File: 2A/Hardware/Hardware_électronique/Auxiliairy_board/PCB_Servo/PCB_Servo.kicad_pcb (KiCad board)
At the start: 2 copper layers, 38.8 x 40.2 mm, 35 parts, among them J10 Conn_ST_STDC14, J9 UART_IN, U1 STM32G071CBUx, U2 AZ1117-3.3

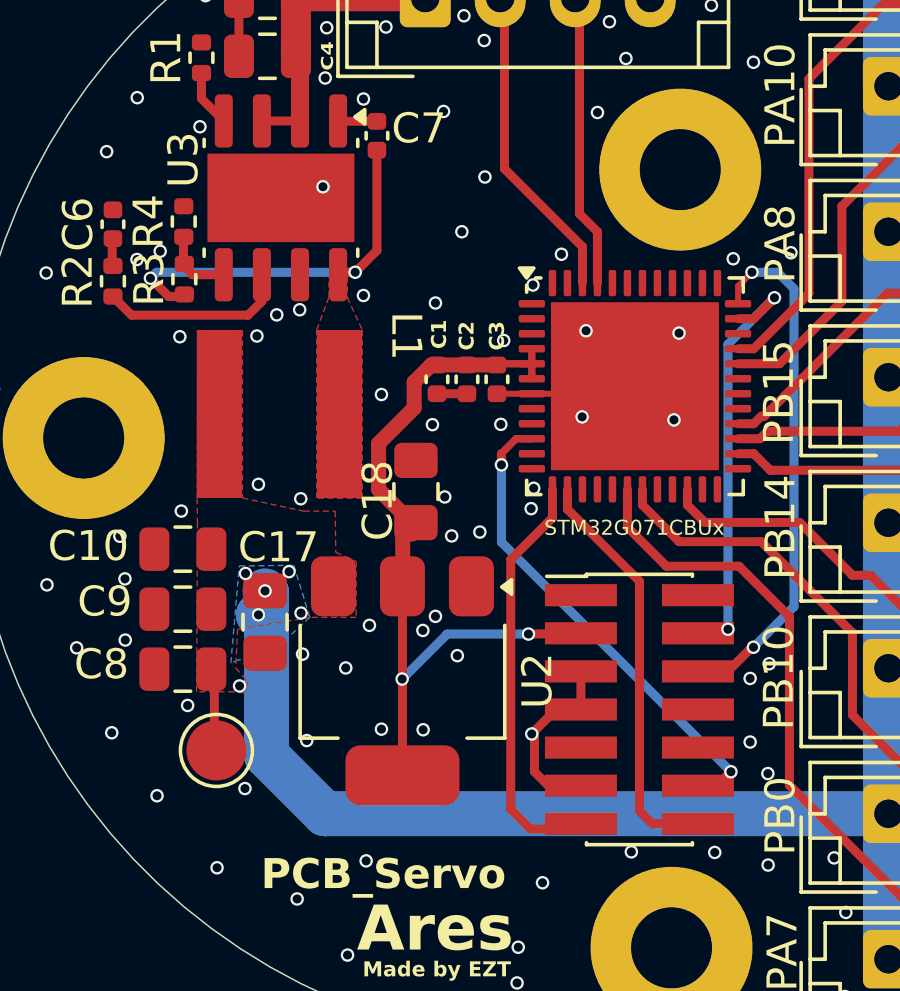
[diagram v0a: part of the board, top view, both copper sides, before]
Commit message: Correction PCB Servo LF
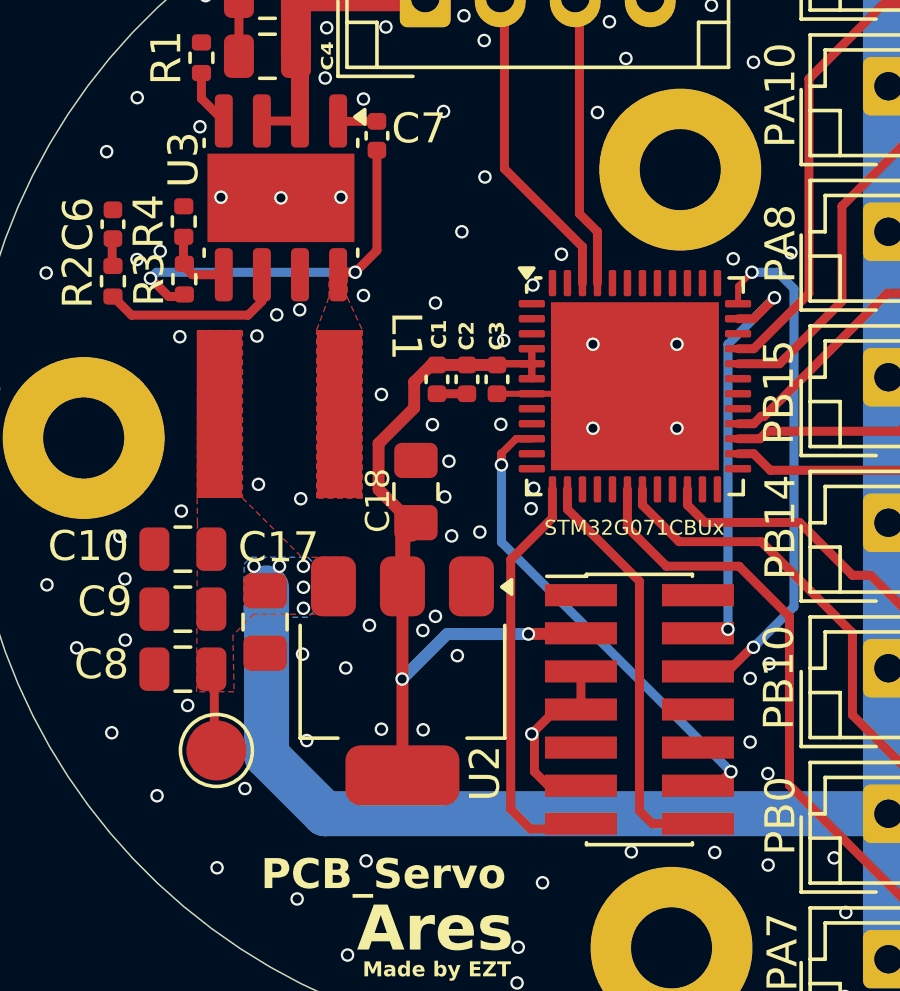
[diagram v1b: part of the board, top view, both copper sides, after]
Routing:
- net +7.5V: track 64.8 -> 64.7 mm, vias 6 -> 5
- net GND: vias 174 -> 177
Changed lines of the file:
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@@
 			(effects
 				(font
-					(size 1 1)
-					(thickness 0.15)
+					(size 0.8 0.8)
+					(thickness 0.13)
 				)
 			)
@@
 		(tags "CMS SOT")
 		(property "Reference" "U2"
-			(at 0 -4.5 90)
+			(at 3.08 -2.75 90)
 			(layer "F.SilkS")
 			(effects
@@
 	)
 	(via
+		(at 137.4 66.8)
+		(size 0.45)
+		(drill 0.3)
+		(layers "F.Cu" "B.Cu")
+		(free yes)
+		(net 1)
+	)
+	(via
 		(at 136.875 62.825)
 		(size 0.45)
@@
 	)
 	(via
-		(at 148.67 71.33)
+		(at 148.6 71.7)
 		(size 0.45)
 		(drill 0.3)
@@
 	)
 	(via
+		(at 133.4 66.8)
+		(size 0.45)
+		(drill 0.3)
+		(layers "F.Cu" "B.Cu")
+		(free yes)
+		(net 1)
+	)
+	(via
 		(at 129.59 65.28)
 		(size 0.45)
@@
 	)
 	(via
+		(at 141 75.6)
+		(size 0.45)
+		(drill 0.3)
+		(layers "F.Cu" "B.Cu")
+		(free yes)
+		(net 1)
+	)
+	(via
 		(at 144.95 58.7)
 		(size 0.45)
@@
 	)
 	(via
-		(at 148.5 74.22)
+		(at 148.6 74.5)
 		(size 0.45)
 		(drill 0.3)
@@
 	)
 	(via
-		(at 136.8 66.45)
+		(at 135.4 66.82)
 		(size 0.45)
 		(drill 0.3)
@@
 	)
 	(via
-		(at 145.44 74.12)
+		(at 145.8 74.5)
 		(size 0.45)
 		(drill 0.3)
@@
 	)
 	(via
-		(at 145.57 71.25)
+		(at 145.8 71.7)
 		(size 0.45)
 		(drill 0.3)
@@
 		(start 145.4 81.335)
 		(end 143.65 81.36)
-		(width 0.3)
+		(width 0.4)
 		(layer "F.Cu")
 		(net 2)
@@
 		(start 138.655 75.008122)
 		(end 138.655 76.5425)
-		(width 0.5)
+		(width 0.4)
 		(layer "F.Cu")
 		(net 2)
@@
 		(start 139.45 82.87)
 		(end 139.44 82.86)
-		(width 0.3)
+		(width 0.4)
 		(layer "F.Cu")
 		(net 2)
@@
 		(start 139.45 82.85)
 		(end 139.45 79.77)
-		(width 0.3)
+		(width 0.4)
 		(layer "F.Cu")
 		(net 2)
@@
 		(start 139.84 72.961734)
 		(end 139.84 73.823122)
-		(width 0.5)
+		(width 0.4)
 		(layer "F.Cu")
 		(net 2)
@@
 		(start 143.645 81.335)
 		(end 143.64 81.33)
-		(width 0.3)
+		(width 0.4)
 		(layer "F.Cu")
 		(net 2)
@@
 		(start 140.411734 72.39)
 		(end 139.84 72.961734)
-		(width 0.5)
+		(width 0.4)
 		(layer "F.Cu")
 		(net 2)
@@
 		(start 138.655 76.5425)
 		(end 139.83 77.7175)
-		(width 0.5)
+		(width 0.4)
 		(layer "F.Cu")
 		(net 2)
@@
 		(start 139.44 82.86)
 		(end 139.45 82.85)
-		(width 0.3)
+		(width 0.4)
 		(layer "F.Cu")
 		(net 2)
@@
 		(start 139.84 73.823122)
 		(end 138.655 75.008122)
-		(width 0.5)
+		(width 0.4)
 		(layer "F.Cu")
 		(net 2)
@@
 		(start 143.65 81.36)
 		(end 143.645 81.335)
-		(width 0.3)
+		(width 0.4)
 		(layer "F.Cu")
 		(net 2)
@@
 		(start 139.45 86.07)
 		(end 139.45 82.87)
-		(width 0.3)
+		(width 0.4)
 		(layer "F.Cu")
 		(net 2)
@@
 		(start 140.6 72.39)
 		(end 142.6 72.39)
-		(width 0.5)
+		(width 0.4)
 		(layer "F.Cu")
 		(net 2)
@@
 		(start 140.6 72.39)
 		(end 140.411734 72.39)
-		(width 0.5)
+		(width 0.4)
 		(layer "F.Cu")
 		(net 2)
@@
 		(start 143.65 81.36)
 		(end 140.94 81.36)
-		(width 0.3)
+		(width 0.4)
 		(layer "B.Cu")
 		(net 2)
@@
 		(start 140.94 81.36)
 		(end 139.44 82.86)
-		(width 0.3)
+		(width 0.4)
 		(layer "B.Cu")
 		(net 2)
@@
 	)
 	(via
-		(at 134.02 83.09)
-		(size 0.45)
-		(drill 0.3)
-		(layers "F.Cu" "B.Cu")
-		(free yes)
-		(net 59)
-	)
-	(via
-		(at 134.22 79.34)
+		(at 134.5 79.1)
 		(size 0.45)
 		(drill 0.3)
@@
 	)
 	(via
-		(at 134.87 79.9225)
+		(at 136.15 79.8)
 		(size 0.45)
 		(drill 0.3)
@@
 	)
 	(via
-		(at 135.67 79.28)
+		(at 136.15 79.1)
 		(size 0.45)
 		(drill 0.3)
@@
 	)
 	(via
-		(at 134.65 80.72)
+		(at 135.35 79.1)
 		(size 0.45)
 		(drill 0.3)
@@
 	)
 	(via
-		(at 136.07 80.66)
+		(at 136.15 80.5)
 		(size 0.45)
 		(drill 0.3)
@@
 	)
 	(segment
-		(start 134.92 80.45)
-		(end 134.65 80.72)
-		(width 1.5)
-		(layer "B.Cu")
-		(net 59)
-	)
-	(segment
 		(start 155.65 82.5)
 		(end 155.65 92.2)
@@
 	)
 	(segment
-		(start 134.87 79.9225)
-		(end 134.92 79.9725)
-		(width 1.5)
-		(layer "B.Cu")
-		(net 59)
-	)
-	(segment
 		(start 155.65 70.95)
 		(end 155.65 74.6)
@@
 	)
 	(segment
-		(start 134.92 80.99)
-		(end 134.92 85.406701)
-		(width 1.5)
-		(layer "B.Cu")
-		(net 59)
-	)
-	(segment
 		(start 134.92 85.406701)
 		(end 136.863299 87.35)
@@
 	)
 	(segment
-		(start 134.92 79.9725)
-		(end 134.92 80.45)
+		(start 134.92 85.406701)
+		(end 134.92 79.82)
 		(width 1.5)
 		(layer "B.Cu")
@@
 		(net 59)
 	)
-	(segment
-		(start 134.65 80.72)
-		(end 134.92 80.99)
-		(width 1.5)
-		(layer "B.Cu")
-		(net 59)
-	)
 	(zone
 		(net 54)
@@
 		(polygon
 			(pts
-				(xy 134.11729 71.243864) (xy 134.11729 76.823864) (xy 136.15729 77.263864) (xy 137.20729 77.263864)
-				(xy 137.22729 78.633864) (xy 137.90729 78.943864) (xy 137.90729 80.803864) (xy 136.38729 80.803864)
-				(xy 133.95729 81.193864) (xy 133.89 82.49) (xy 134.29 82.94) (xy 134.18 83.32) (xy 133.83729 83.283864)
-				(xy 132.58729 83.283864) (xy 132.61729 77.673864) (xy 132.60729 76.813864) (xy 132.62729 71.243864)
+				(xy 134.11729 71.243864) (xy 134.11729 76.823864) (xy 136.1 78.8) (xy 137.5 78.8) (xy 137.5 80.7)
+				(xy 134.5 80.7) (xy 133.8 81.4) (xy 133.83729 83.283864) (xy 132.58729 83.283864) (xy 132.61729 77.673864)
+				(xy 132.60729 76.813864) (xy 132.62729 71.243864)
 			)
 		)
@@
 	)
 	(zone
-		(net 0)
-		(net_name "")
+		(net 59)
+		(net_name "+7.5V")
 		(layer "B.Cu")
 		(hatch edge 0.5)
-		(connect_pads yes
+		(priority 3)
+		(connect_pads
 			(clearance 0)
 		)
 		(min_thickness 0.25)
 		(filled_areas_thickness no)
-		(keepout
-			(tracks allowed)
-			(vias allowed)
-			(pads allowed)
-			(copperpour not_allowed)
-			(footprints allowed)
-		)
-		(fill
+		(fill yes
 			(thermal_gap 0.5)
 			(thermal_bridge_width 0.5)
@@
 		(polygon
 			(pts
-				(xy 156.8 80.525) (xy 157.625 81.35) (xy 157.6 81.375)
+				(xy 134.4 78.8) (xy 136.3 78.8) (xy 136.5 79) (xy 136.5 80.6) (xy 136.3 80.8) (xy 134.4 80.8) (xy 134.17 80.6)
+				(xy 134.17 79.03)
 			)
 		)
 	)
 	(zone
-		(net 59)
-		(net_name "+7.5V")
+		(net 0)
+		(net_name "")
 		(layer "B.Cu")
-		(name "SW")
 		(hatch edge 0.5)
-		(priority 3)
 		(connect_pads yes
 			(clearance 0)
@@
 		(min_thickness 0.25)
 		(filled_areas_thickness no)
-		(fill yes
+		(keepout
+			(tracks allowed)
+			(vias allowed)
+			(pads allowed)
+			(copperpour not_allowed)
+			(footprints allowed)
+		)
+		(fill
 			(thermal_gap 0.5)
 			(thermal_bridge_width 0.5)
@@
 		(polygon
 			(pts
-				(xy 133.73 82.33) (xy 134.01 79.09) (xy 135.83 79.07) (xy 136.36 80.8) (xy 135.01 82.06) (xy 133.99 82.22)
+				(xy 156.8 80.525) (xy 157.625 81.35) (xy 157.6 81.375)
 			)
 		)
